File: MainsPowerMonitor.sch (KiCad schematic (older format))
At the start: 11 parts, among them J401 Screw_Terminal_01x02, J402 AudioJack2_SwitchT

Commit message: started routing backing up tonnes of changes,2.048V reference changed to 2.5V ref, to match ucc2800, cos to change to a version with a 2V feedback, would require me to update the Oscillator cap and resistor,and also recalulate the class 2 loop compensation components etc.  Move the location of the teensy LC and added the ESP-WROOM-o2 wifi module.
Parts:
- J402: symbol Connector:AudioJack3_Switch -> Connector:AudioJack3
- R401: value 7.5K ohms .1% -> 5.9K ohms .1%
- R404: value 33 Ohms 0.1% -> 41.2 Ohms 0.1%
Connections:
- net labels added: +2.5V_REF
- net labels removed: +2.048V_REF
- wire segments 59 -> 49
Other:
- note added: "1.25V"
- note added: "2.481V at 392V Mains"
- note added: "2.486V at Peak current"
- note added: "This transformer could be replaced with \nTi's isolated precision amplifier: AMC1100\nsee slaa552.pdf"
- note removed: "1.024V"
- note removed: "2.014V at Peak current"
- note removed: "2.027V at 392V Mains"
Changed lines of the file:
@@
 P 3650 3800
 F 0 "R401" H 3709 3846 50  0000 L CNN
-F 1 "7.5K ohms .1%" H 3709 3755 50  0000 L CNN
+F 1 "5.9K ohms .1%" H 3709 3755 50  0000 L CNN
 F 2 "Resistors_SMD:R_0805_HandSoldering" H 3650 3800 50  0001 C CNN
 F 3 "~" H 3650 3800 50  0001 C CNN
@@
 	4600 4600 4600 4550
 Text Notes 4850 4650 0    50   ~ 0
-1.024V
+1.25V
 Connection ~ 3650 3950
 Wire Wire Line
@@
 P 4300 3200
 F 0 "R404" H 4359 3246 50  0000 L CNN
-F 1 "33 Ohms 0.1%" H 4359 3155 50  0000 L CNN
+F 1 "41.2 Ohms 0.1%" H 4359 3155 50  0000 L CNN
 F 2 "Resistors_SMD:R_0805_HandSoldering" H 4300 3200 50  0001 C CNN
 F 3 "~" H 4300 3200 50  0001 C CNN
@@
 	4300 4600 4600 4600
 $Comp
-L Connector:AudioJack3_Switch J402
+L Connector:AudioJack3 J402
 U 1 1 5F18094B
-P 3450 2900
-F 0 "J402" H 3400 3350 50  0000 C CNN
-F 1 "AudioJack2_SwitchT" H 3450 3250 50  0000 C CNN
-F 2 "Connect_jl:Audio_StereoJack_3.5mm_ASJ-99H-R-HT-T" H 3450 2900 50  0001 C CNN
-F 3 "http://www.adam-tech.com/downloader.php?p=ASJ-99H-X-HT-TR.pdf" H 3450 2900 50  0001 C CNN
-	1    3450 2900
+P 3400 2900
+F 0 "J402" H 3350 3350 50  0000 C CNN
+F 1 "AudioJack2_SwitchT" H 3400 3250 50  0000 C CNN
+F 2 "Connect_jl:Audio_StereoJack_3.5mm_ASJ-99H-R-HT-T" H 3400 2900 50  0001 C CNN
+F 3 "http://www.adam-tech.com/downloader.php?p=ASJ-99H-X-HT-TR.pdf" H 3400 2900 50  0001 C CNN
+	1    3400 2900
 	1    0    0    1
 $EndComp
@@
 	5350 3950 6150 3950
 Text Notes 6600 2950 2    50   ~ 0
-2.014V at Peak current
+2.486V at Peak current
 Text Notes 6900 3850 2    50   ~ 0
-2.027V at 392V Mains
-Wire Wire Line
-	4300 3300 4300 3500
-Wire Wire Line
-	3650 3100 3950 3100
-Wire Wire Line
-	4000 3100 4000 3500
-Wire Wire Line
-	4000 3500 4050 3500
-Connection ~ 4300 3500
-Wire Wire Line
-	4300 3500 4300 4600
-Wire Wire Line
-	3650 2700 3950 2700
-Wire Wire Line
-	4300 2700 4300 3050
-Connection ~ 4300 3050
-Wire Wire Line
-	3650 2900 3950 2900
-Wire Wire Line
-	3950 2900 3950 2700
-Connection ~ 3950 2700
-Wire Wire Line
-	3950 2700 4300 2700
-Wire Wire Line
-	3650 3000 3950 3000
-Wire Wire Line
-	3950 3000 3950 3100
-Connection ~ 3950 3100
-Wire Wire Line
-	3950 3100 4000 3100
-Wire Wire Line
-	3650 2600 4150 2600
-Wire Wire Line
-	4150 2600 4150 3500
-Connection ~ 4150 3500
-Wire Wire Line
-	4150 3500 4300 3500
-Wire Wire Line
-	3650 2800 4050 2800
-Wire Wire Line
-	4050 2800 4050 3500
-Connection ~ 4050 3500
-Wire Wire Line
-	4050 3500 4150 3500
+2.481V at 392V Mains
 Text Notes 2650 3400 0    50   ~ 0
 46:1
@@
 Connection ~ 3650 4500
 Text HLabel 4750 4050 2    50   Input ~ 0
-+2.048V_REF
++2.5V_REF
 Wire Wire Line
 	4750 4050 4600 4050
 Wire Wire Line
 	4600 4050 4600 4350
+Text Notes 1200 4650 0    50   ~ 0
+This transformer could be replaced with \nTi's isolated precision amplifier: AMC1100\nsee slaa552.pdf
+Wire Wire Line
+	4300 3300 4300 3450
+Wire Wire Line
+	3600 3000 3950 3000
+Wire Wire Line
+	3950 3000 3950 3450
+Wire Wire Line
+	3950 3450 4300 3450
+Connection ~ 4300 3450
+Wire Wire Line
+	4300 3450 4300 4600
+Wire Wire Line
+	3600 2800 4300 2800
+Wire Wire Line
+	4300 2800 4300 2900
+Connection ~ 4300 3050
+Wire Wire Line
+	3600 2900 4300 2900
+Connection ~ 4300 2900
+Wire Wire Line
+	4300 2900 4300 3050
 $EndSCHEMATC

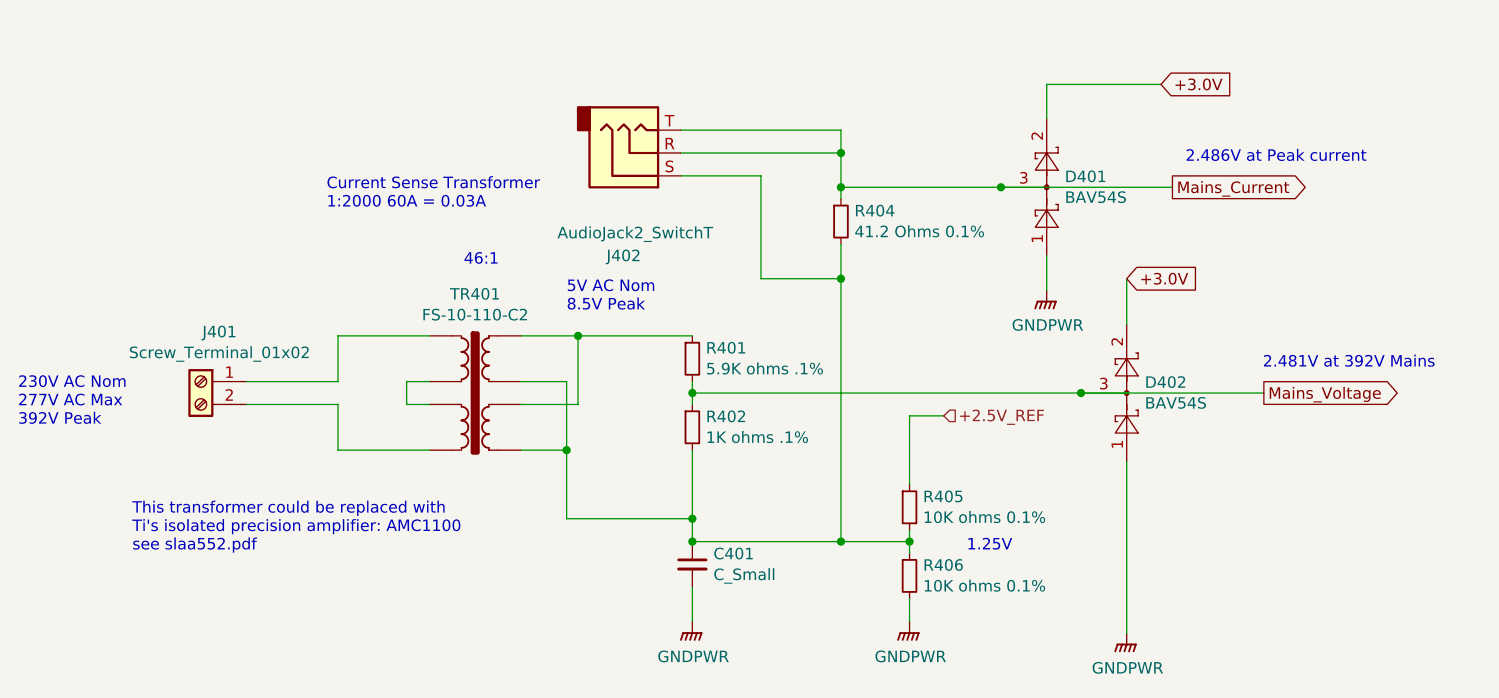
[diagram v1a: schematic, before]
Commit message: Consolidated a lot of part values that were the same part but not detected the same by Boms_away BOM editor because of subtle differences in how I specified the values. Added Digi-key part numbers to the resistors. Replaced 2mOhm .5W current sense resistors with 1W 2mOhm Thin Film resistors (lower inductance than metal element), And fixed a bug where I was earthing the return feed of the Solar inverter before passing through the current sense resistor.
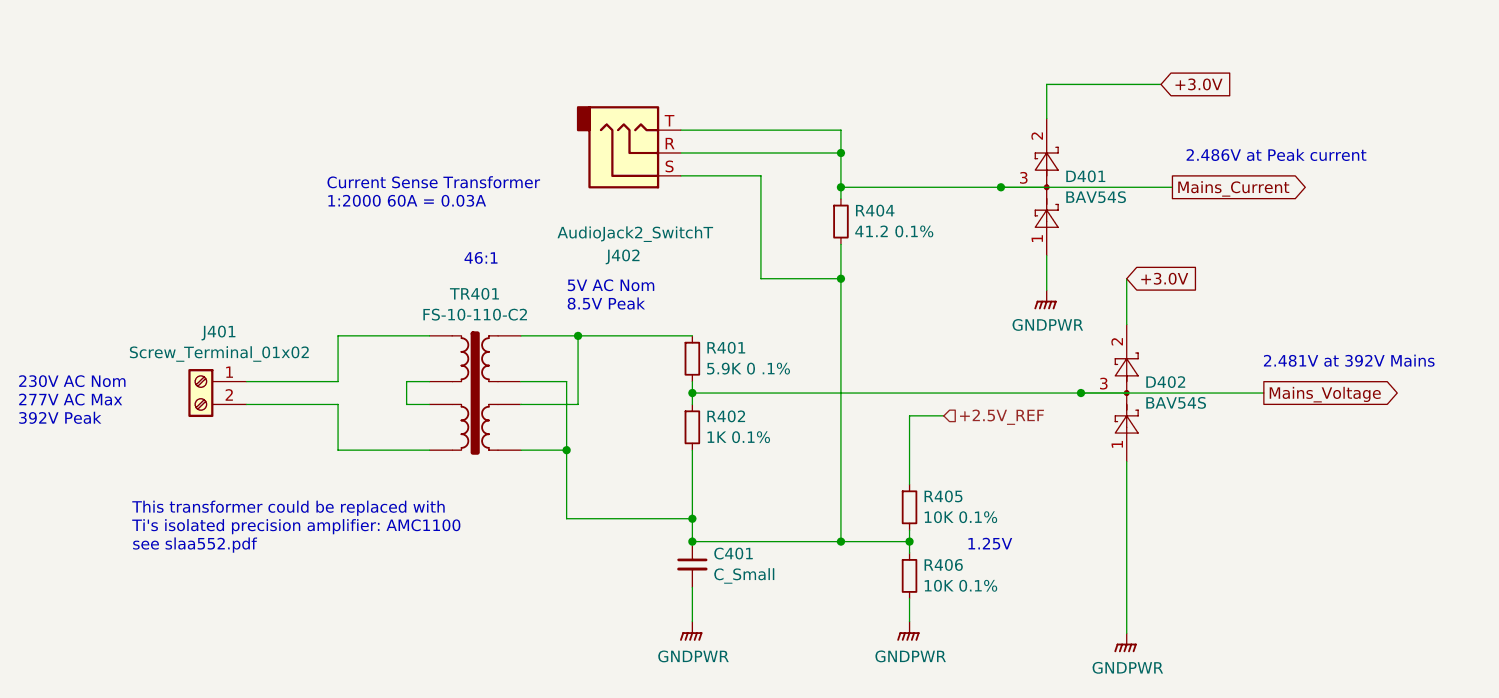
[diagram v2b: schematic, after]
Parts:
- C401, D401, D402, J401, J402, TR401: MFR (none) -> -; MPN (none) -> -; SPN (none) -> -; SPR (none) -> -; SPURL (none) -> -
- R401: value 5.9K ohms .1% -> 5.9K 0 .1%; MFR (none) -> Panasonic Electronic Components; MPN (none) -> ERA-6AEB5901V; SPN (none) -> P5.9KDACT-ND; SPR (none) -> digikey; SPURL (none) -> -
- R402: value 1K ohms .1% -> 1K 0.1%; MFR (none) -> Panasonic Electronic Components; MPN (none) -> ERA-6AEB102V; SPN (none) -> P1.0KDACT-ND; SPR (none) -> digikey; SPURL (none) -> -
- R404: value 41.2 Ohms 0.1% -> 41.2 0.1%; MFR (none) -> Panasonic Electronic Components; MPN (none) -> ERA-6AEB4122V; SPN (none) -> P41.2KDACT-ND; SPR (none) -> digikey; SPURL (none) -> -
- R405, R406: value 10K ohms 0.1% -> 10K 0.1%; MFR (none) -> Panasonic Electronic Components; MPN (none) -> ERA-6AEB103V; SPN (none) -> P10KDACT-ND; SPR (none) -> digikey; SPURL (none) -> -

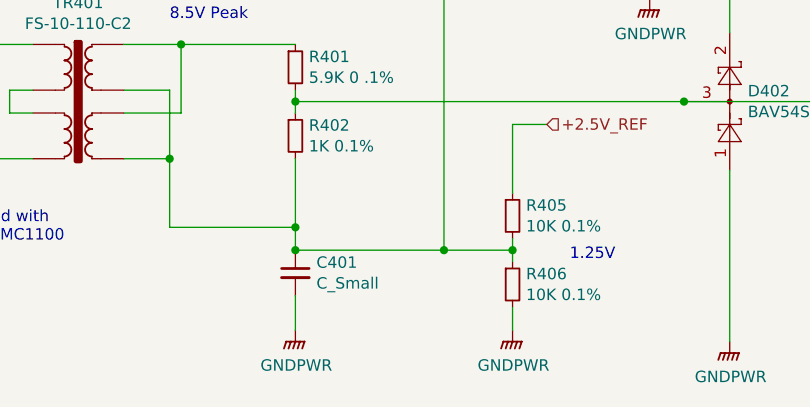
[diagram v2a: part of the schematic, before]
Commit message: change a few compoents foot prints for SOT23 to SOT23-Handsoldered, and SOT23-5 to SOT23-5-Handsoldered
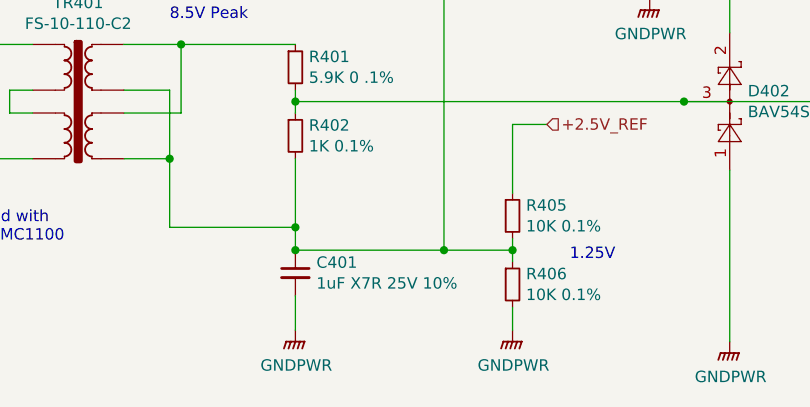
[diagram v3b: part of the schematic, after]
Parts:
- C401: value C_Small -> 1uF X7R 25V 10%; MFR - -> Wurth Elektronik; MPN - -> 885012207078; SPN - -> 732-7672-1-ND; SPR - -> digikey
- D401, D402: footprint Package_TO_SOT_SMD:SOT-23 -> Package_TO_SOT_SMD:SOT-23_Handsoldering

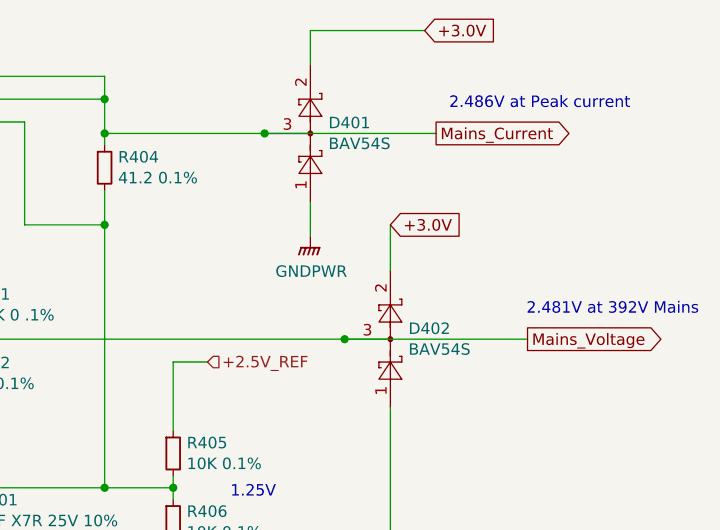
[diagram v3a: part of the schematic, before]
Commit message: Finished adding digi key part numbers, for now git add *
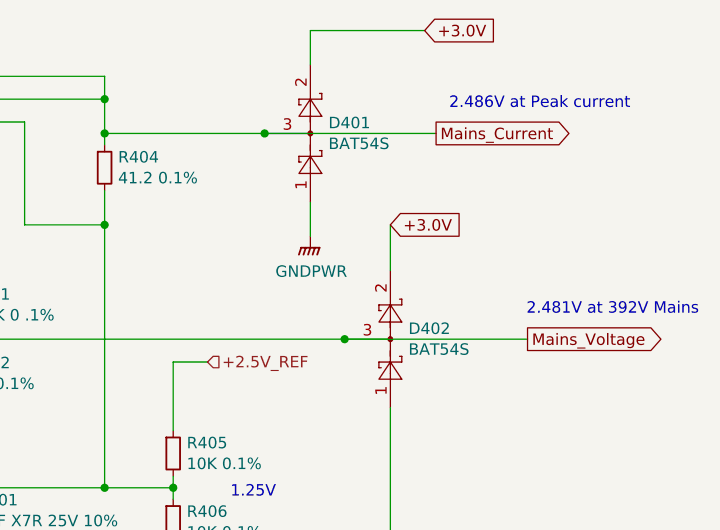
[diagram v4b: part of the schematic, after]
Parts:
- D401, D402: value BAV54S -> BAT54S; MFR - -> Toshiba Semiconductor and Storage; MPN - -> TBAT54S,LM; SPN - -> TBAT54SLMCT-ND; SPR - -> digikey
- J401: MFR - -> Phoenix Contact; MPN - -> 1792863; SPN - -> 277-2518-ND; SPR - -> digikey
- J402: MFR - -> Adam Tech; MPN - -> ASJ-99H-R-HT-T/R; SPN - -> 2057-ASJ-99H-R-HT-T/RCT-ND; SPR - -> digikey
- TR401: MFR - -> Triad Magnetics; MPN - -> FS10-110-C2; SPN - -> 237-1578-ND; SPR - -> digikey
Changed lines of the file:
@@
 F 2 "Transformers_ThroughHole_jl:FS10-110-C2" H 2700 4000 50 0001 C CNN
 F 3 "http://catalog.triadmagnetics.com/Asset/FS10-110-C2.pdf" H 2700 4000 50 0001 C CNN
-F 4 "-" H 0 0 50 0001 C CNN "MFR"
-F 5 "-" H 0 0 50 0001 C CNN "MPN"
-F 6 "-" H 0 0 50 0001 C CNN "SPR"
-F 7 "-" H 0 0 50 0001 C CNN "SPN"
+F 4 "Triad Magnetics" H 0 0 50 0001 C CNN "MFR"
+F 5 "FS10-110-C2" H 0 0 50 0001 C CNN "MPN"
+F 6 "digikey" H 0 0 50 0001 C CNN "SPR"
+F 7 "237-1578-ND" H 0 0 50 0001 C CNN "SPN"
 F 8 "-" H 0 0 50 0001 C CNN "SPURL"
 	1    2700 4000
@@
 F 2 "digikey-footprints:Term_Block_1x2_P5mm" H 1500 3900 50 0001 C CNN
 F 3 "https://media.digikey.com/pdf/Data%20Sheets/Phoenix%20Contact%20PDFs/1792863.pdf" H 1500 3900 50 0001 C CNN
-F 4 "-" H 0 0 50 0001 C CNN "MFR"
-F 5 "-" H 0 0 50 0001 C CNN "MPN"
-F 6 "-" H 0 0 50 0001 C CNN "SPR"
-F 7 "-" H 0 0 50 0001 C CNN "SPN"
+F 4 "Phoenix Contact" H 0 0 50 0001 C CNN "MFR"
+F 5 "1792863" H 0 0 50 0001 C CNN "MPN"
+F 6 "digikey" H 0 0 50 0001 C CNN "SPR"
+F 7 "277-2518-ND" H 0 0 50 0001 C CNN "SPN"
 F 8 "-" H 0 0 50 0001 C CNN "SPURL"
 	1    1500 3900
@@
 F 2 "Connect_jl:Audio_StereoJack_3.5mm_ASJ-99H-R-HT-T" H 3400 2900 50 0001 C CNN
 F 3 "http://www.adam-tech.com/downloader.php?p=ASJ-99H-X-HT-TR.pdf" H 3400 2900 50 0001 C CNN
-F 4 "-" H 0 0 50 0001 C CNN "MFR"
-F 5 "-" H 0 0 50 0001 C CNN "MPN"
-F 6 "-" H 0 0 50 0001 C CNN "SPR"
-F 7 "-" H 0 0 50 0001 C CNN "SPN"
+F 4 "Adam Tech" H 0 0 50 0001 C CNN "MFR"
+F 5 "ASJ-99H-R-HT-T/R" H 0 0 50 0001 C CNN "MPN"
+F 6 "digikey" H 0 0 50 0001 C CNN "SPR"
+F 7 "2057-ASJ-99H-R-HT-T/RCT-ND" H 0 0 50 0001 C CNN "SPN"
 F 8 "-" H 0 0 50 0001 C CNN "SPURL"
 	1    3400 2900
@@
 P 5200 3050
 F 0 "D401" V 5246 3129 50 0000 L CNN
-F 1 "BAV54S" V 5155 3129 50 0000 L CNN
+F 1 "BAT54S" V 5155 3129 50 0000 L CNN
 F 2 "Package_TO_SOT_SMD:SOT-23_Handsoldering" H 5200 2550 50 0001 C CNN
-F 3 "https://assets.nexperia.com/documents/data-sheet/BAT54_SER.pdf" H 5200 3050 50 0001 C CNN
-F 4 "-" H 0 0 50 0001 C CNN "MFR"
-F 5 "-" H 0 0 50 0001 C CNN "MPN"
-F 6 "-" H 0 0 50 0001 C CNN "SPR"
-F 7 "-" H 0 0 50 0001 C CNN "SPN"
+F 3 "http://toshiba.semicon-storage.com/info/docget.jsp?did=37137&prodName=TBAT54" H 5200 3050 50 0001 C CNN
+F 4 "Toshiba Semiconductor and Storage" H 0 0 50 0001 C CNN "MFR"
+F 5 "TBAT54S,LM" H 0 0 50 0001 C CNN "MPN"
+F 6 "digikey" H 0 0 50 0001 C CNN "SPR"
+F 7 "TBAT54SLMCT-ND" H 0 0 50 0001 C CNN "SPN"
 F 8 "-" H 0 0 50 0001 C CNN "SPURL"
 	1    5200 3050
@@
 P 5550 3950
 F 0 "D402" V 5596 4029 50 0000 L CNN
-F 1 "BAV54S" V 5505 4029 50 0000 L CNN
+F 1 "BAT54S" V 5505 4029 50 0000 L CNN
 F 2 "Package_TO_SOT_SMD:SOT-23_Handsoldering" H 5550 3450 50 0001 C CNN
-F 3 "https://assets.nexperia.com/documents/data-sheet/BAT54_SER.pdf" H 5550 3950 50 0001 C CNN
-F 4 "-" H 0 0 50 0001 C CNN "MFR"
-F 5 "-" H 0 0 50 0001 C CNN "MPN"
-F 6 "-" H 0 0 50 0001 C CNN "SPR"
-F 7 "-" H 0 0 50 0001 C CNN "SPN"
+F 3 "http://toshiba.semicon-storage.com/info/docget.jsp?did=37137&prodName=TBAT54" H 5550 3950 50 0001 C CNN
+F 4 "Toshiba Semiconductor and Storage" H 0 0 50 0001 C CNN "MFR"
+F 5 "TBAT54S,LM" H 0 0 50 0001 C CNN "MPN"
+F 6 "digikey" H 0 0 50 0001 C CNN "SPR"
+F 7 "TBAT54SLMCT-ND" H 0 0 50 0001 C CNN "SPN"
 F 8 "-" H 0 0 50 0001 C CNN "SPURL"
 	1    5550 3950

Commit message: Change footprint for the main switching FET to have a bent drain to achieve trace width and clearance requirements.  Fixed a pin numbering miss alignment between schematic and footprint for the isolating transformer. Spoted trace clearance issue on the 230V AC mains input into the isolating transformer for the house voltage sense, increased to 2.5mm.
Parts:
- TR401: symbol Transformer:TRANSF6 -> CustomDevice:TRANSF6
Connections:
- net AC_Mains_Phase: now reaches J401.1 (Pin_1), TR401.1
- net AC_Mains_Neutral: now reaches J401.2 (Pin_2), TR401.4
- net at C401.1, J402.S, R402.2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: now also TR401.6, TR401.8; no longer TR401.5, TR401.7
- new net: R401.1, TR401.5, TR401.7
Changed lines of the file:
@@
 $EndDescr
 $Comp
-L Transformer:TRANSF6 TR401
+L CustomDevice:TRANSF6 TR401
 U 1 1 5F15E54A
-P 2700 4000
-F 0 "TR401" H 2700 4482 50  0000 C CNN
-F 1 "FS-10-110-C2" H 2700 4391 50  0000 C CNN
-F 2 "Transformers_ThroughHole_jl:FS10-110-C2" H 2700 4000 50  0001 C CNN
-F 3 "http://catalog.triadmagnetics.com/Asset/FS10-110-C2.pdf" H 2700 4000 50  0001 C CNN
-F 4 "Triad Magnetics" H 0   0   50  0001 C CNN "MFR"
-F 5 "FS10-110-C2" H 0   0   50  0001 C CNN "MPN"
-F 6 "digikey" H 0   0   50  0001 C CNN "SPR"
-F 7 "237-1578-ND" H 0   0   50  0001 C CNN "SPN"
-F 8 "-" H 0   0   50  0001 C CNN "SPURL"
-	1    2700 4000
+P 2700 3950
+F 0 "TR401" H 2700 4432 50  0000 C CNN
+F 1 "FS-10-110-C2" H 2700 4341 50  0000 C CNN
+F 2 "Transformers_ThroughHole_jl:FS10-110-C2" H 2700 3950 50  0001 C CNN
+F 3 "http://catalog.triadmagnetics.com/Asset/FS10-110-C2.pdf" H 2700 3950 50  0001 C CNN
+F 4 "Triad Magnetics" H 0   -50 50  0001 C CNN "MFR"
+F 5 "FS10-110-C2" H 0   -50 50  0001 C CNN "MPN"
+F 6 "digikey" H 0   -50 50  0001 C CNN "SPR"
+F 7 "237-1578-ND" H 0   -50 50  0001 C CNN "SPN"
+F 8 "-" H 0   -50 50  0001 C CNN "SPURL"
+	1    2700 3950
 	1    0    0    -1
 $EndComp
@@
 Connection ~ 4300 3050
 Connection ~ 4300 2900
+Text Label 1750 3900 0    50   ~ 0
+AC_Mains_Phase
+Text Label 1750 4000 0    50   ~ 0
+AC_Mains_Neutral
 $EndSCHEMATC

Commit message: Found that my local updates of Kicad footprint librarys, had changed the names of resistor and capacitor footprints, so I updated all these footprint names.  Added circuit to measure the Vin via pin 28 of the Teensy-LC, This will allow the battery system to shut down if the battery voltage gets too low.
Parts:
- C401: footprint Capacitors_SMD:C_0805_HandSoldering -> Capacitor_SMD:C_0805_2012Metric_Pad1.15x1.40mm_HandSolder
- R401, R402, R404, R405, R406: footprint Resistors_SMD:R_0805_HandSoldering -> Resistor_SMD:R_0805_2012Metric_Pad1.15x1.40mm_HandSolder
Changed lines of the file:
@@
 F 0 "R401" H 3709 3846 50  0000 L CNN
 F 1 "5.9K 0 .1%" H 3709 3755 50  0000 L CNN
-F 2 "Resistors_SMD:R_0805_HandSoldering" H 3650 3800 50  0001 C CNN
+F 2 "Resistor_SMD:R_0805_2012Metric_Pad1.15x1.40mm_HandSolder" H 3650 3800 50  0001 C CNN
 F 3 "https://industrial.panasonic.com/cdbs/www-data/pdf/RDM0000/AOA0000C307.pdf" H 3650 3800 50  0001 C CNN
 F 4 "Panasonic Electronic Components" H 0   0   50  0001 C CNN "MFR"
@@
 F 0 "R402" H 3709 4146 50  0000 L CNN
 F 1 "1K 0.1%" H 3709 4055 50  0000 L CNN
-F 2 "Resistors_SMD:R_0805_HandSoldering" H 3650 4100 50  0001 C CNN
+F 2 "Resistor_SMD:R_0805_2012Metric_Pad1.15x1.40mm_HandSolder" H 3650 4100 50  0001 C CNN
 F 3 "https://industrial.panasonic.com/cdbs/www-data/pdf/RDM0000/AOA0000C307.pdf" H 3650 4100 50  0001 C CNN
 F 4 "Panasonic Electronic Components" H 0   0   50  0001 C CNN "MFR"
@@
 F 0 "C401" H 3742 4746 50  0000 L CNN
 F 1 "1uF X7R 25V 10%" H 3742 4655 50  0000 L CNN
-F 2 "Capacitors_SMD:C_0805_HandSoldering" H 3650 4700 50  0001 C CNN
+F 2 "Capacitor_SMD:C_0805_2012Metric_Pad1.15x1.40mm_HandSolder" H 3650 4700 50  0001 C CNN
 F 3 "~" H 3650 4700 50  0001 C CNN
 F 4 "Wurth Elektronik" H 0   0   50  0001 C CNN "MFR"
@@
 F 0 "R405" H 4659 4496 50  0000 L CNN
 F 1 "10K 0.1%" H 4659 4405 50  0000 L CNN
-F 2 "Resistors_SMD:R_0805_HandSoldering" H 4600 4450 50  0001 C CNN
+F 2 "Resistor_SMD:R_0805_2012Metric_Pad1.15x1.40mm_HandSolder" H 4600 4450 50  0001 C CNN
 F 3 "https://industrial.panasonic.com/cdbs/www-data/pdf/RDM0000/AOA0000C307.pdf" H 4600 4450 50  0001 C CNN
 F 4 "Panasonic Electronic Components" H 0   0   50  0001 C CNN "MFR"
@@
 F 0 "R406" H 4659 4796 50  0000 L CNN
 F 1 "10K 0.1%" H 4659 4705 50  0000 L CNN
-F 2 "Resistors_SMD:R_0805_HandSoldering" H 4600 4750 50  0001 C CNN
+F 2 "Resistor_SMD:R_0805_2012Metric_Pad1.15x1.40mm_HandSolder" H 4600 4750 50  0001 C CNN
 F 3 "https://industrial.panasonic.com/cdbs/www-data/pdf/RDM0000/AOA0000C307.pdf" H 4600 4750 50  0001 C CNN
 F 4 "Panasonic Electronic Components" H 0   0   50  0001 C CNN "MFR"
@@
 F 0 "R404" H 4359 3246 50  0000 L CNN
 F 1 "41.2  0.1%" H 4359 3155 50  0000 L CNN
-F 2 "Resistors_SMD:R_0805_HandSoldering" H 4300 3200 50  0001 C CNN
+F 2 "Resistor_SMD:R_0805_2012Metric_Pad1.15x1.40mm_HandSolder" H 4300 3200 50  0001 C CNN
 F 3 "https://industrial.panasonic.com/cdbs/www-data/pdf/RDM0000/AOA0000C307.pdf" H 4300 3200 50  0001 C CNN
 F 4 "Panasonic Electronic Components" H 0   0   50  0001 C CNN "MFR"
